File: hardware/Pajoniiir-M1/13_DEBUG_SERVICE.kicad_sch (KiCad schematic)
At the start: 15 parts

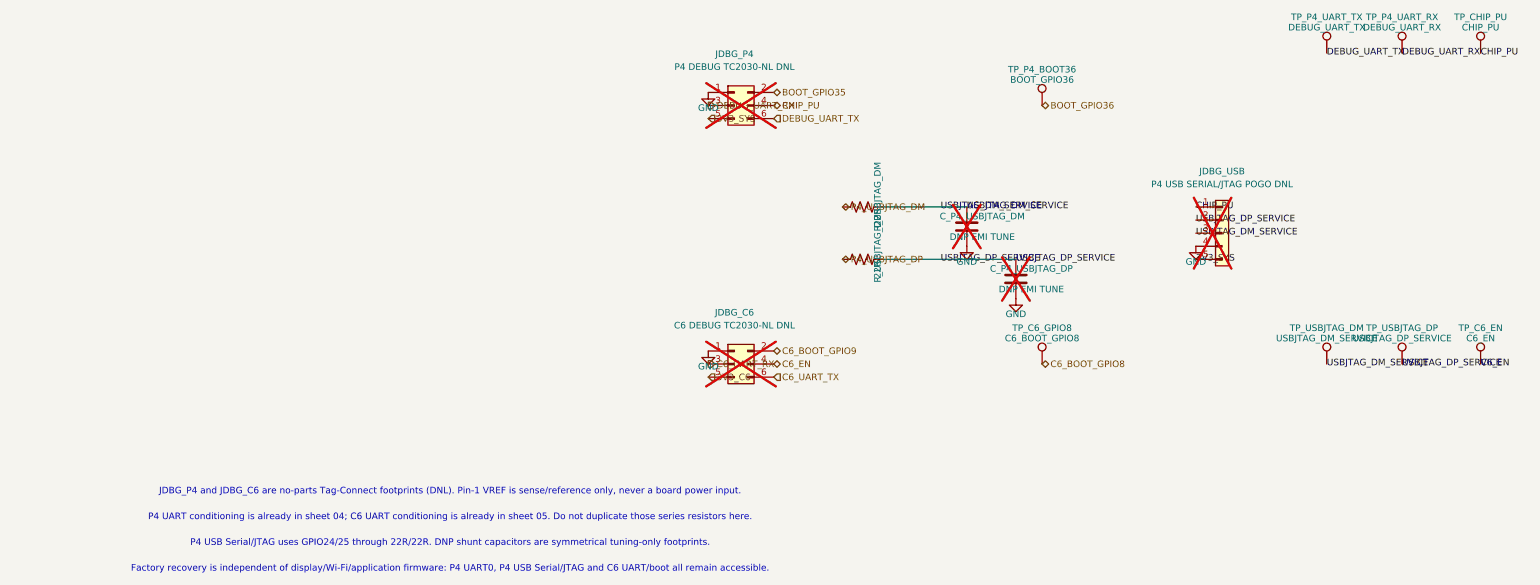
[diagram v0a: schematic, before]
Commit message: hardware: normalize schematic reference designators
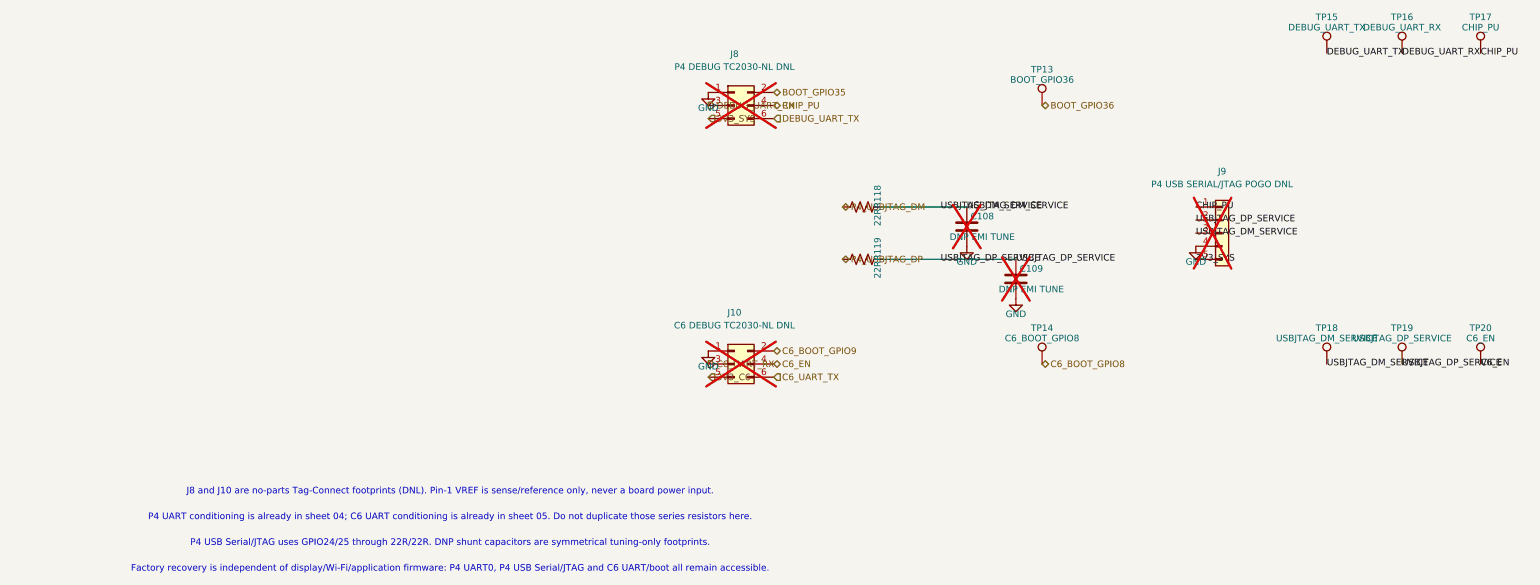
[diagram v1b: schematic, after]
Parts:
- renumbered C_P4_USBJTAG_DM to C108, C_P4_USBJTAG_DP to C109, JDBG_C6 to J10, JDBG_P4 to J8, JDBG_USB to J9, R_USBJTAG_DM to R118, R_USBJTAG_DP to R119, TP_P4_BOOT36 to TP13, TP_C6_GPIO8 to TP14, TP_P4_UART_TX to TP15, TP_P4_UART_RX to TP16, TP_CHIP_PU to TP17, TP_USBJTAG_DM to TP18, TP_USBJTAG_DP to TP19, TP_C6_EN to TP20
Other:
- note added: "J8 and J10 are no-parts Tag-Connect footprints (DNL). Pin-1 VREF is sense/reference only, never a board power input."
- note removed: "JDBG_P4 and JDBG_C6 are no-parts Tag-Connect footprints (DNL). Pin-1 VREF is sense/reference only, never a board power input."

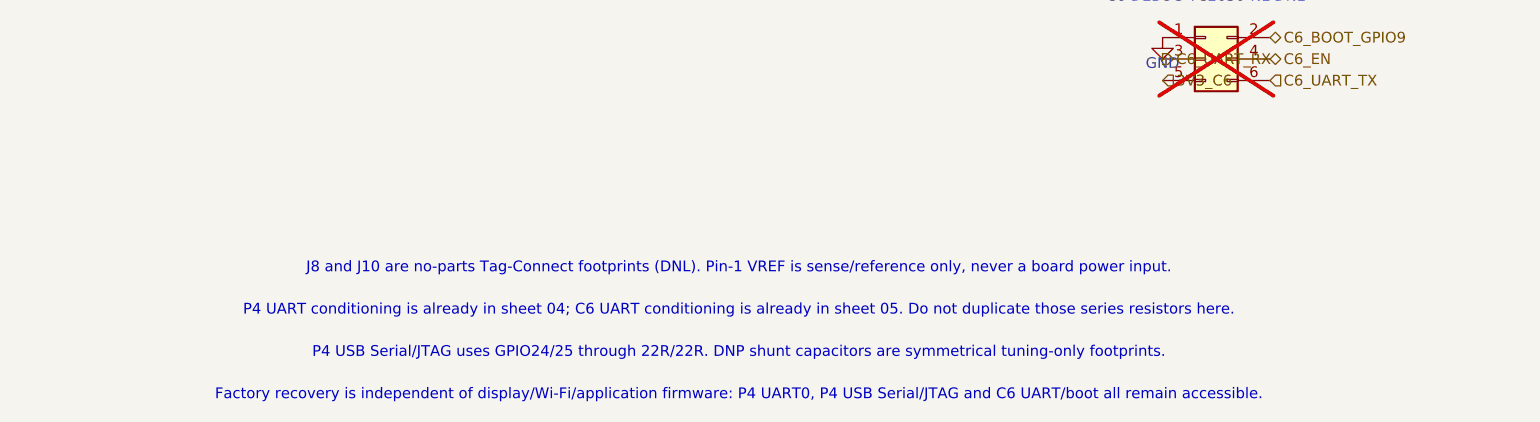
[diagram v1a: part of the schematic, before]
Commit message: hardware: constrain RefDes migration to annotation fields
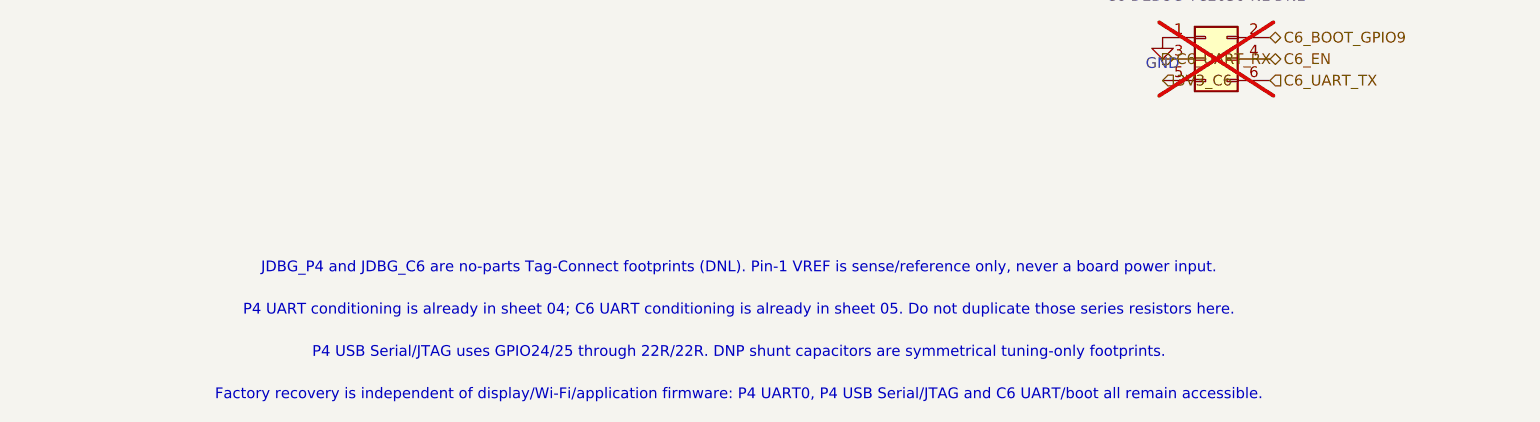
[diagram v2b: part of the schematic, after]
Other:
- note added: "JDBG_P4 and JDBG_C6 are no-parts Tag-Connect footprints (DNL). Pin-1 VREF is sense/reference only, never a board power input."
- note removed: "J8 and J10 are no-parts Tag-Connect footprints (DNL). Pin-1 VREF is sense/reference only, never a board power input."
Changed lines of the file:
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@@
     (lib_id "power:GND") (at 85.09 42.545 0) (unit 1)
     (exclude_from_sim no) (in_bom yes) (on_board yes) (dnp no)
-    (property "Reference" "#PWR_J8_5" (at 85.09 48.545 0) (effects (font (size 1.27 1.27)) (hide yes)))
+    (property "Reference" "#PWR_JDBG_P4_5" (at 85.09 48.545 0) (effects (font (size 1.27 1.27)) (hide yes)))
     (property "Value" "GND" (at 85.09 45.545 0) (effects (font (size 1.27 1.27))))
     (property "Footprint" "" (at 85.09 42.545 0) (effects (font (size 1.27 1.27)) (hide yes)))
     (property "Datasheet" "" (at 85.09 42.545 0) (effects (font (size 1.27 1.27)) (hide yes)))
     (pin "1")
-    (instances (project "Pajoniiir-M1" (path "/2c8dd352-b7b8-4d9e-8f93-5dd43be2a100/3100000d-6b2a-4a3a-8c91-00000000000d" (reference "#PWR_J8_5") (unit 1))))
+    (instances (project "Pajoniiir-M1" (path "/2c8dd352-b7b8-4d9e-8f93-5dd43be2a100/3100000d-6b2a-4a3a-8c91-00000000000d" (reference "#PWR_JDBG_P4_5") (unit 1))))
   )
   (symbol
@@
     (lib_id "power:GND") (at 85.09 92.71 0) (unit 1)
     (exclude_from_sim no) (in_bom yes) (on_board yes) (dnp no)
-    (property "Reference" "#PWR_J10_5" (at 85.09 98.71 0) (effects (font (size 1.27 1.27)) (hide yes)))
+    (property "Reference" "#PWR_JDBG_C6_5" (at 85.09 98.71 0) (effects (font (size 1.27 1.27)) (hide yes)))
     (property "Value" "GND" (at 85.09 95.71 0) (effects (font (size 1.27 1.27))))
     (property "Footprint" "" (at 85.09 92.71 0) (effects (font (size 1.27 1.27)) (hide yes)))
     (property "Datasheet" "" (at 85.09 92.71 0) (effects (font (size 1.27 1.27)) (hide yes)))
     (pin "1")
-    (instances (project "Pajoniiir-M1" (path "/2c8dd352-b7b8-4d9e-8f93-5dd43be2a100/3100000d-6b2a-4a3a-8c91-00000000000d" (reference "#PWR_J10_5") (unit 1))))
+    (instances (project "Pajoniiir-M1" (path "/2c8dd352-b7b8-4d9e-8f93-5dd43be2a100/3100000d-6b2a-4a3a-8c91-00000000000d" (reference "#PWR_JDBG_C6_5") (unit 1))))
   )
   (symbol
@@
   )
   (label "C6_EN" (at 234.95 95.25 0) (effects (font (size 1.27 1.27))))
-  (text "J8 and J10 are no-parts Tag-Connect footprints (DNL). Pin-1 VREF is sense/reference only, never a board power input." (exclude_from_sim no) (at 35 120 0) (effects (font (size 1.27 1.27))))
+  (text "JDBG_P4 and JDBG_C6 are no-parts Tag-Connect footprints (DNL). Pin-1 VREF is sense/reference only, never a board power input." (exclude_from_sim no) (at 35 120 0) (effects (font (size 1.27 1.27))))
   (text "P4 UART conditioning is already in sheet 04; C6 UART conditioning is already in sheet 05. Do not duplicate those series resistors here." (exclude_from_sim no) (at 35 125 0) (effects (font (size 1.27 1.27))))
   (text "P4 USB Serial/JTAG uses GPIO24/25 through 22R/22R. DNP shunt capacitors are symmetrical tuning-only footprints." (exclude_from_sim no) (at 35 130 0) (effects (font (size 1.27 1.27))))
